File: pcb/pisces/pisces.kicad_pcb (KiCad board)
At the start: 2 copper layers, 41 parts, among them SW1 SW_PUSH, SW10 SW_PUSH, SW11 SW_PUSH, SW12 SW_PUSH, SW13 SW_PUSH, SW14 SW_PUSH, SW15 SW_PUSH, SW16 SW_PUSH, SW17 SW_PUSH, SW18 SW_PUSH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

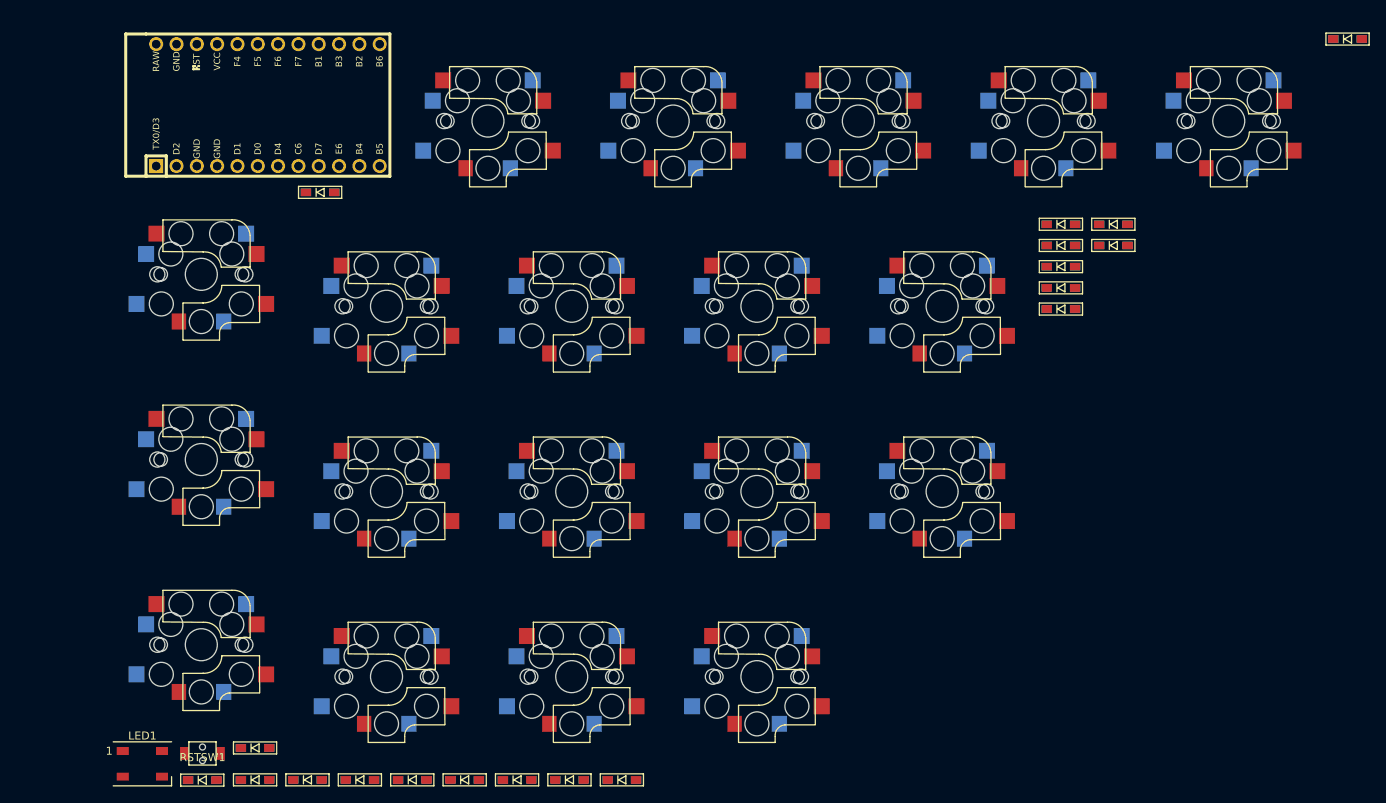
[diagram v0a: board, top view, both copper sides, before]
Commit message: Fixed the switches, diodes, and mounting holes' position
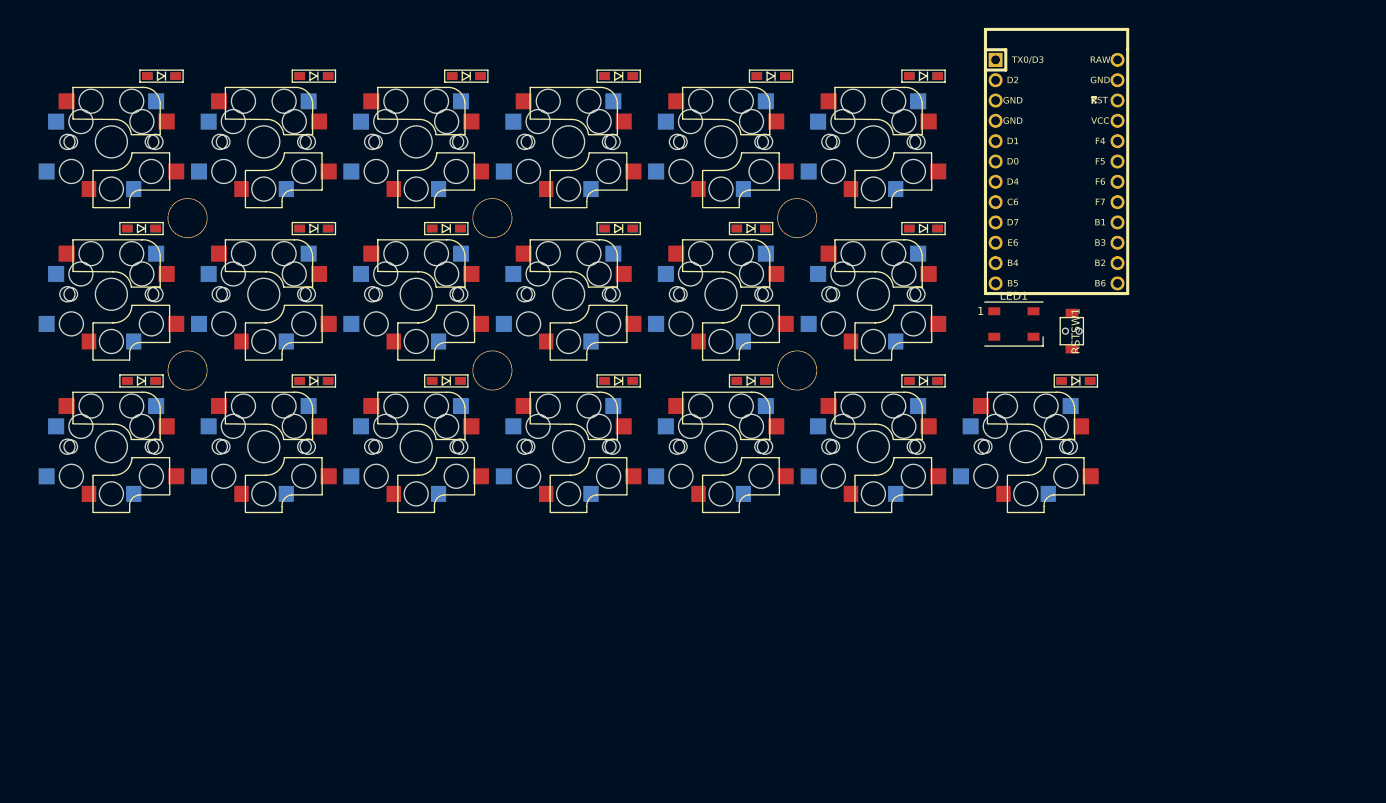
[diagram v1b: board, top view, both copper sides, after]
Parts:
- added HOLE1: Val**, kbd:HOLE, F.Cu at (59.5, 59.5)
- added HOLE13: Val**, kbd:HOLE, F.Cu at (135.7, 59.5)
- added HOLE14: Val**, kbd:HOLE, F.Cu at (135.7, 78.6)
- added HOLE2: Val**, kbd:HOLE, F.Cu at (59.5, 78.6)
- added HOLE7: Val**, kbd:HOLE, F.Cu at (97.6, 59.5)
- added HOLE8: Val**, kbd:HOLE, F.Cu at (97.6, 78.6)
- moved SW3 145.5 mm to (50.0, 88.1)
- moved LED1 122.0 mm to (162.8, 72.8)
- moved RSTSW1 120.8 mm to (170.1, 73.7), turned to 90 degrees
- moved D19 120.1 mm to (170.6, 79.9), turned to 180 degrees
- moved D8 115.1 mm to (91.9, 60.8), turned to 180 degrees
- moved D2 114.9 mm to (53.8, 60.8), turned to 180 degrees
- moved D16 112.7 mm to (151.5, 41.8), turned to 180 degrees
- moved D17 103.3 mm to (151.5, 60.8), turned to 180 degrees
- moved D6 101.4 mm to (75.3, 79.9), turned to 180 degrees
- moved U1 98.9 mm to (168.1, 53.7), turned to 270 degrees
- moved D4 97.8 mm to (75.3, 41.8), turned to 180 degrees
- moved D18 97.3 mm to (151.5, 79.9), turned to 180 degrees
- moved SW2 93.8 mm to (50.0, 69.0)
- moved D5 93.7 mm to (75.3, 60.8), turned to 180 degrees
- moved D7 88.9 mm to (94.4, 41.8), turned to 180 degrees
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
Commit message: Connected row/col/switches tracks
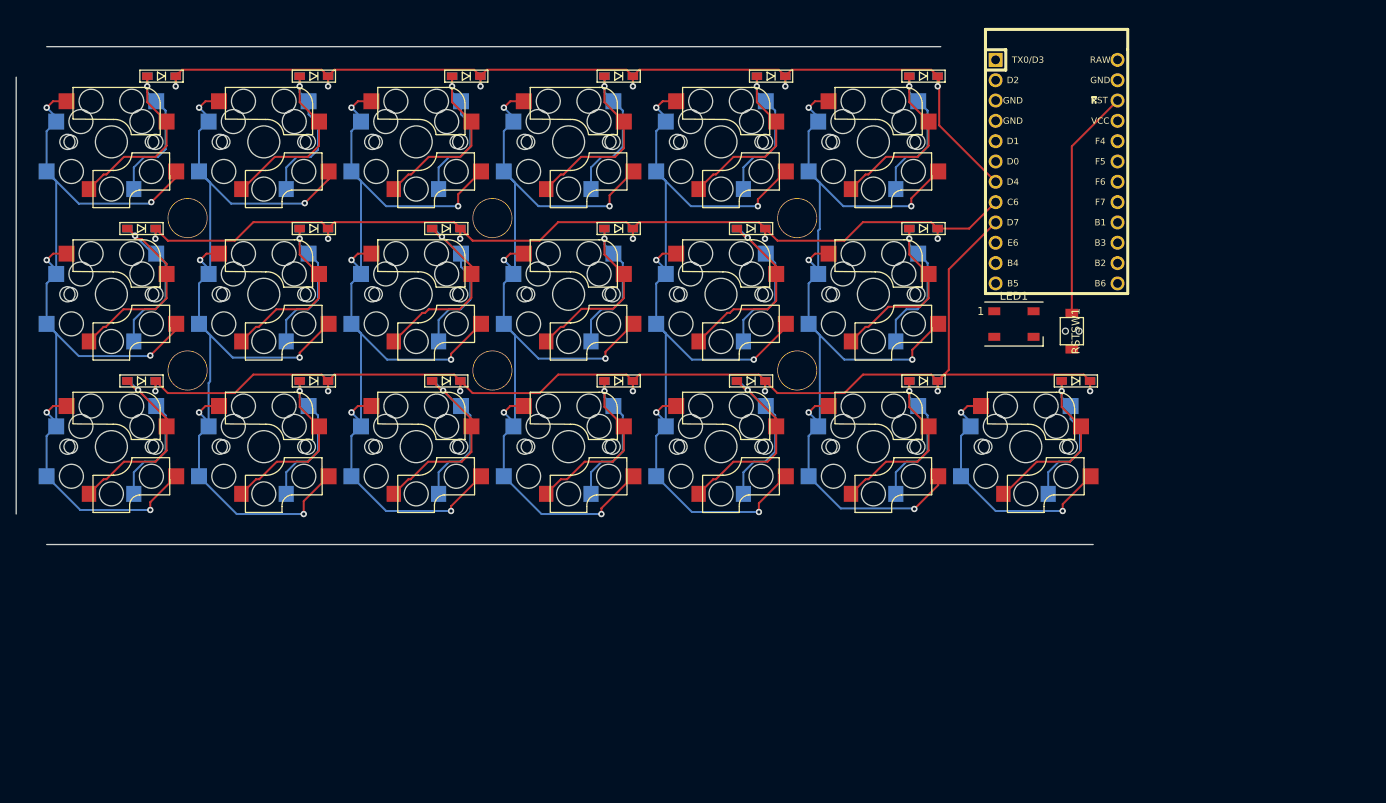
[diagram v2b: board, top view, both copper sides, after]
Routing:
- net row2: track 0.00 -> 165.2 mm, vias 0 -> 7
- net row0: track 0.00 -> 130.0 mm, vias 0 -> 6
- net row1: track 0.00 -> 128.8 mm, vias 0 -> 6
- net col3: track 0.00 -> 123.7 mm, vias 0 -> 6
- net col5: track 0.00 -> 123.5 mm, vias 0 -> 6
- net col1: track 0.00 -> 123.3 mm, vias 0 -> 6
- net col2: track 0.00 -> 123.1 mm, vias 0 -> 6
- net col4: track 0.00 -> 123.0 mm, vias 0 -> 6
- net col0: track 0.00 -> 122.2 mm, vias 0 -> 6
- net Net-(D2-Pad2): track 0.00 -> 42.0 mm, vias 0 -> 1
- net Net-(D14-Pad2): track 0.00 -> 42.0 mm, vias 0 -> 1
- net Net-(D15-Pad2): track 0.00 -> 41.8 mm, vias 0 -> 1
- net Net-(D9-Pad2): track 0.00 -> 41.7 mm, vias 0 -> 1
- net Net-(D3-Pad2): track 0.00 -> 41.6 mm, vias 0 -> 1
- net Net-(D8-Pad2): track 0.00 -> 41.6 mm, vias 0 -> 1
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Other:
- board outline added: 134.6 x 62.2 mm

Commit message: Rough Edge.Cut drawing
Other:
- board size 134.6 x 62.2 mm -> 142.2 x 66 mm
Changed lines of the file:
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@@
   (general
     (thickness 1.6)
-    (drawings 3)
+    (drawings 8)
     (tracks 833)
     (zones 0)
@@
     )
   )
-  (gr_line (start 41.91 38.1) (end 153.67 38.1) (layer Edge.Cuts) (width 0.05))
-  (gr_line (start 41.91 100.33) (end 172.72 100.33) (layer Edge.Cuts) (width 0.05))
-  (gr_line (start 38.1 41.91) (end 38.1 96.52) (layer Edge.Cuts) (width 0.05))
+  (gr_arc (start 41.91 38.1) (end 41.91 34.29) (angle -90) (layer Edge.Cuts) (width 0.05))
+  (gr_arc (start 176.53 38.1) (end 180.34 38.1) (angle -90) (layer Edge.Cuts) (width 0.05))
+  (gr_arc (start 176.53 96.52) (end 176.53 100.33) (angle -90) (layer Edge.Cuts) (width 0.05))
+  (gr_arc (start 41.91 96.52) (end 38.1 96.52) (angle -90) (layer Edge.Cuts) (width 0.05))
+  (gr_line (start 176.53 34.29) (end 41.91 34.29) (layer Edge.Cuts) (width 0.05))
+  (gr_line (start 180.34 96.52) (end 180.34 38.1) (layer Edge.Cuts) (width 0.05))
+  (gr_line (start 41.91 100.33) (end 176.53 100.33) (layer Edge.Cuts) (width 0.05))
+  (gr_line (start 38.1 38.1) (end 38.1 96.52) (layer Edge.Cuts) (width 0.05))
   (via (at 54.483 43.053) (size 0.8) (drill 0.4) (layers F.Cu B.Cu) (net 1))
   (segment (start 54.486 43.05) (end 54.483 43.053) (width 0.25) (layer F.Cu) (net 1))

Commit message: Connected all tracks other than GND
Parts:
- moved RSTSW1 5.87 mm to (175.9, 73.1), turned to 0 degrees
- moved LED1 5.35 mm to (168.1, 73.2), turned to 180 degrees
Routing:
- net col0: track 122.2 -> 270.4 mm
- net col1: track 123.3 -> 252.2 mm
- net col2: track 123.1 -> 234.7 mm
- net col3: track 123.7 -> 218.1 mm
- net col4: track 123.0 -> 200.1 mm
- net col5: track 123.5 -> 183.3 mm
- net led: track 0.00 -> 37.1 mm
- net VCC: track 0.00 -> 29.5 mm
- net col6: track 32.1 -> 60.3 mm, vias 2 -> 3
